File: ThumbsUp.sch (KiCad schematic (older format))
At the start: 138 parts, among them J1 Conn_01x04_Male, J10 Raiser_Male, J11 Raiser_Female, J12 Raiser_Male, J13 Raiser_Female, J14 Raiser_Male, J15 Raiser_Female, J16 Raiser_Male, J17 Raiser_Female, J18 Raiser_Male, J19 52559-1233, J2 Conn_01x04_Male, J20 Conn_01x04_Female, J21 Conn_01x04_Female, J22 Conn_01x04_Female, J23 Conn_01x04_Female, J24 Conn_01x04_Male, J25 Conn_01x04_Male, J26 Conn_01x04_Male, J27 Conn_01x04_Male, J28 Conn_01x04_Female, J29 Conn_01x04_Female, J3 Conn_01x04_Female, J30 Conn_01x04_Female, J31 Conn_01x04_Female, J4 Conn_01x04_Male, J5 Conn_01x04_Female, J6 Conn_01x04_Male, J7 Conn_01x04_Male, J8 Conn_01x04_Male, J9 Raiser_Female, SW1 SW_Push, U1 ATmega32U4-AU, Y1 16MHz

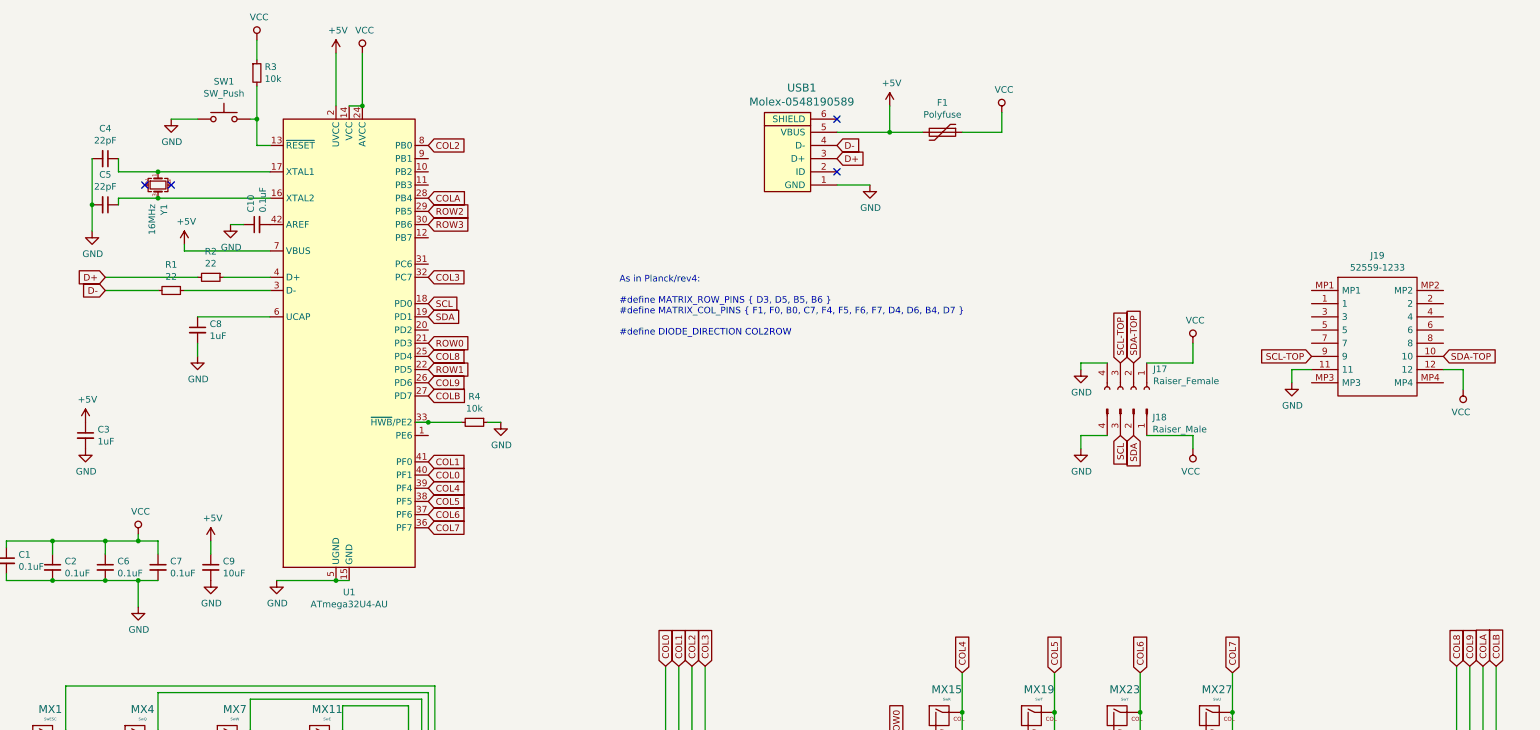
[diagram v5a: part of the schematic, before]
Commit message: Moved the tracks from under MCU
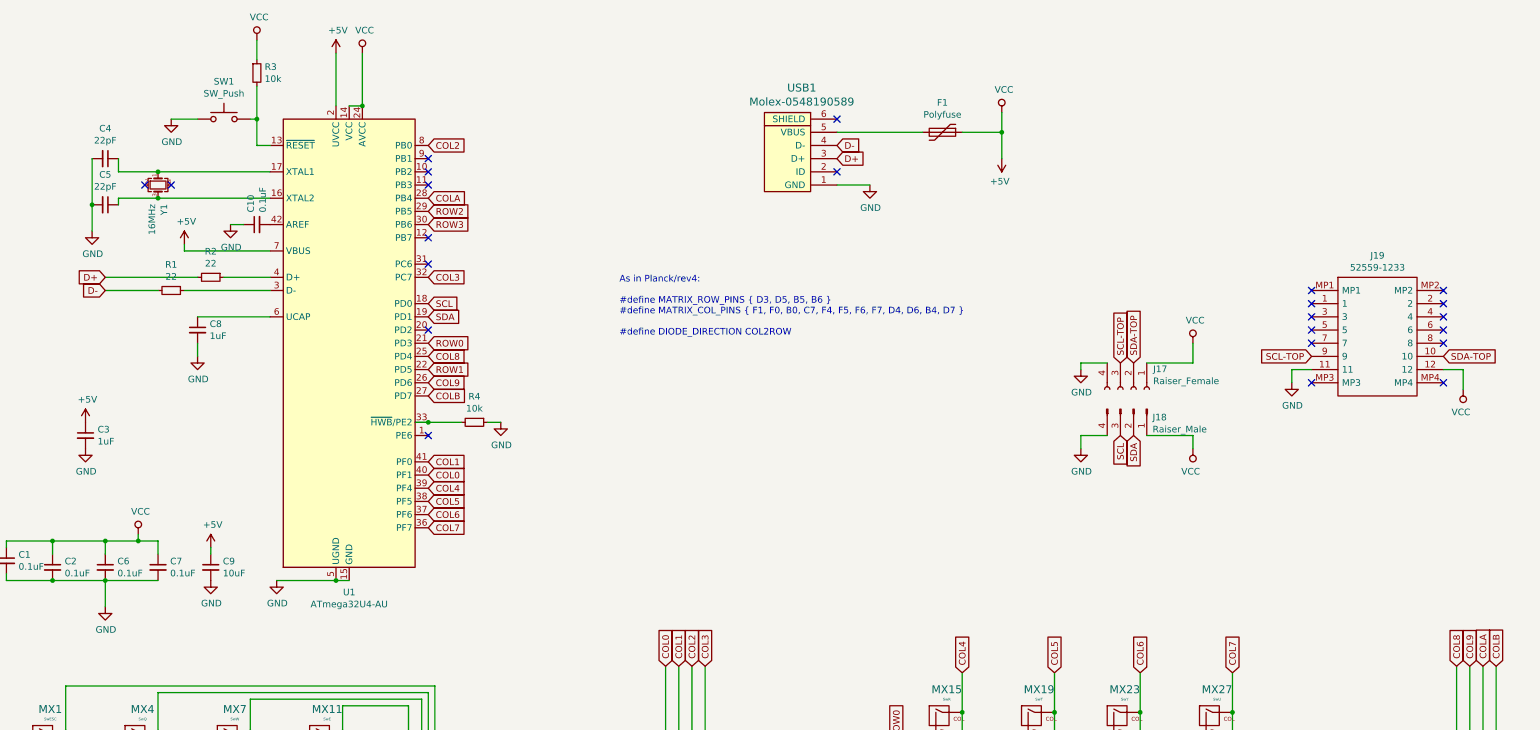
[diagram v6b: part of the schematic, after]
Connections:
- net VCC is gone; now on net +5V: C1.1, C2.1, C6.1, C7.1, F1.1, J17.1 (Pin_1), J18.1 (Pin_1), J19.12, R3.1, U1.14 (VCC), U1.24 (AVCC), U1.34 (VCC), U1.44 (AVCC)
- net +5V: no longer F1.2, USB1.5 (VBUS)
- new net: F1.2, USB1.5 (VBUS)
- no-connect marks 36 -> 55
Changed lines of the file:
@@
-	1    0    0    -1
-$EndComp
-$Comp
-L power:GND #PWR05
-U 1 1 616BEA7C
-P 2000 5750
-F 0 "#PWR05" H 2000 5500 50  0001 C CNN
-F 1 "GND" H 2005 5577 50  0000 C CNN
-F 2 "" H 2000 5750 50  0001 C CNN
-F 3 "" H 2000 5750 50  0001 C CNN
-	1    2000 5750
 	1    0    0    -1
 $EndComp
@@
 Connection ~ 2000 5250
 Wire Wire Line
-	2550 5250 2550 5350
-Wire Wire Line
-	2150 5550 2000 5550
-Wire Wire Line
-	2000 5550 2000 5750
-Wire Wire Line
-	2000 5550 1750 5550
-Connection ~ 2000 5550
+	2550 5300 2550 5350
 Wire Wire Line
 	1750 5550 1350 5550
@@
 $EndComp
 Wire Wire Line
-	7300 2150 7700 2150
-Wire Wire Line
-	7700 1950 7700 2150
-Connection ~ 7700 2150
-Wire Wire Line
-	7700 2150 7950 2150
+	8550 2350 8550 2150
 Wire Wire Line
 	8550 2000 8550 2150
@@
 	1    0    0    -1
 $EndComp
-Wire Wire Line
-	7300 2550 7550 2550
 Text GLabel 7300 2250 2    50   Input ~ 0
 D-
 Text GLabel 7300 2350 2    50   Input ~ 0
 D+
-Wire Wire Line
-	3700 1950 3600 1950
 Text GLabel 4200 3750 2    50   Input ~ 0
 ROW0
@@
 L power:+5V #PWR018
 U 1 1 61D515F6
-P 7700 1950
-F 0 "#PWR018" H 7700 1800 50  0001 C CNN
-F 1 "+5V" H 7715 2123 50  0000 C CNN
-F 2 "" H 7700 1950 50  0001 C CNN
-F 3 "" H 7700 1950 50  0001 C CNN
-	1    7700 1950
-	1    0    0    -1
+P 8550 2350
+F 0 "#PWR018" H 8550 2200 50  0001 C CNN
+F 1 "+5V" H 8565 2523 50  0000 C CNN
+F 2 "" H 8550 2350 50  0001 C CNN
+F 3 "" H 8550 2350 50  0001 C CNN
+	1    8550 2350
+	-1   0    0    1
 $EndComp
 $Comp
@@
 	1    0    0    -1
 $EndComp
-Wire Wire Line
-	3700 1550 3700 1950
 $Comp
 L power:VCC #PWR015
@@
 	1    0    0    -1
 $EndComp
-Wire Wire Line
-	3500 1550 3500 1950
 $Comp
 L power:VCC #PWR012
@@
 $EndComp
 Wire Wire Line
-	2350 3050 2350 3000
-Wire Wire Line
 	2350 3050 3000 3050
 $Comp
@@
 	1    0    0    -1
 $EndComp
-Wire Wire Line
-	2800 2850 2700 2850
 $Comp
 L power:GND #PWR016
@@
 L power:+5V #PWR09
 U 1 1 61E33E14
-P 2550 5250
-F 0 "#PWR09" H 2550 5100 50  0001 C CNN
-F 1 "+5V" H 2565 5423 50  0000 C CNN
-F 2 "" H 2550 5250 50  0001 C CNN
-F 3 "" H 2550 5250 50  0001 C CNN
-	1    2550 5250
+P 2550 5300
+F 0 "#PWR09" H 2550 5150 50  0001 C CNN
+F 1 "+5V" H 2565 5473 50  0000 C CNN
+F 2 "" H 2550 5300 50  0001 C CNN
+F 3 "" H 2550 5300 50  0001 C CNN
+	1    2550 5300
 	1    0    0    -1
 $EndComp
@@
 Connection ~ 4200 4350
 Wire Wire Line
-	3050 5550 3500 5550
-Wire Wire Line
-	3500 5550 3600 5550
-Connection ~ 3500 5550
-Connection ~ 3700 1950
-Wire Wire Line
 	4650 4350 4750 4350
 Wire Wire Line
@@
 	9650 4450 10000 4450
 Wire Wire Line
-	10000 4450 10000 4550
-Wire Wire Line
 	9350 3900 9150 3900
 Wire Wire Line
@@
 Wire Wire Line
 	9350 4450 9150 4450
-Wire Wire Line
-	9150 4450 9150 4550
 $Comp
 L Connector:Conn_01x04_Male J7
@@
 Wire Wire Line
 	10300 6550 10300 7350
+Wire Wire Line
+	7300 2150 7950 2150
+Connection ~ 8550 2150
+NoConn ~ 4200 2350
+NoConn ~ 4200 2450
+NoConn ~ 4200 2550
+NoConn ~ 4200 2950
+NoConn ~ 4200 3150
+NoConn ~ 4200 3650
+NoConn ~ 4200 4450
+NoConn ~ 11900 3350
+NoConn ~ 11900 3450
+NoConn ~ 11900 3550
+NoConn ~ 11900 3650
+NoConn ~ 11900 3750
+NoConn ~ 11900 4050
+NoConn ~ 10900 3350
+NoConn ~ 10900 3450
+NoConn ~ 10900 3550
+NoConn ~ 10900 3650
+NoConn ~ 10900 3750
+NoConn ~ 10900 4050
+Wire Wire Line
+	3050 5550 3500 5550
+Connection ~ 3500 5550
+Wire Wire Line
+	3500 5550 3600 5550
+Wire Wire Line
+	3700 1550 3700 1950
+Wire Wire Line
+	3700 1950 3600 1950
+Connection ~ 3700 1950
+Wire Wire Line
+	1750 5550 2150 5550
+$Comp
+L power:GND #PWR05
+U 1 1 616BEA7C
+P 1750 5750
+F 0 "#PWR05" H 1750 5500 50  0001 C CNN
+F 1 "GND" H 1755 5577 50  0000 C CNN
+F 2 "" H 1750 5750 50  0001 C CNN
+F 3 "" H 1750 5750 50  0001 C CNN
+	1    1750 5750
+	1    0    0    -1
+$EndComp
+Wire Wire Line
+	1750 5750 1750 5550
+Wire Wire Line
+	7300 2550 7550 2550
+Wire Wire Line
+	10000 4450 10000 4550
+Wire Wire Line
+	9150 4450 9150 4550
+Wire Wire Line
+	3500 1550 3500 1950
+Wire Wire Line
+	2350 3050 2350 3000
+Wire Wire Line
+	2700 2850 2800 2850
 $EndSCHEMATC

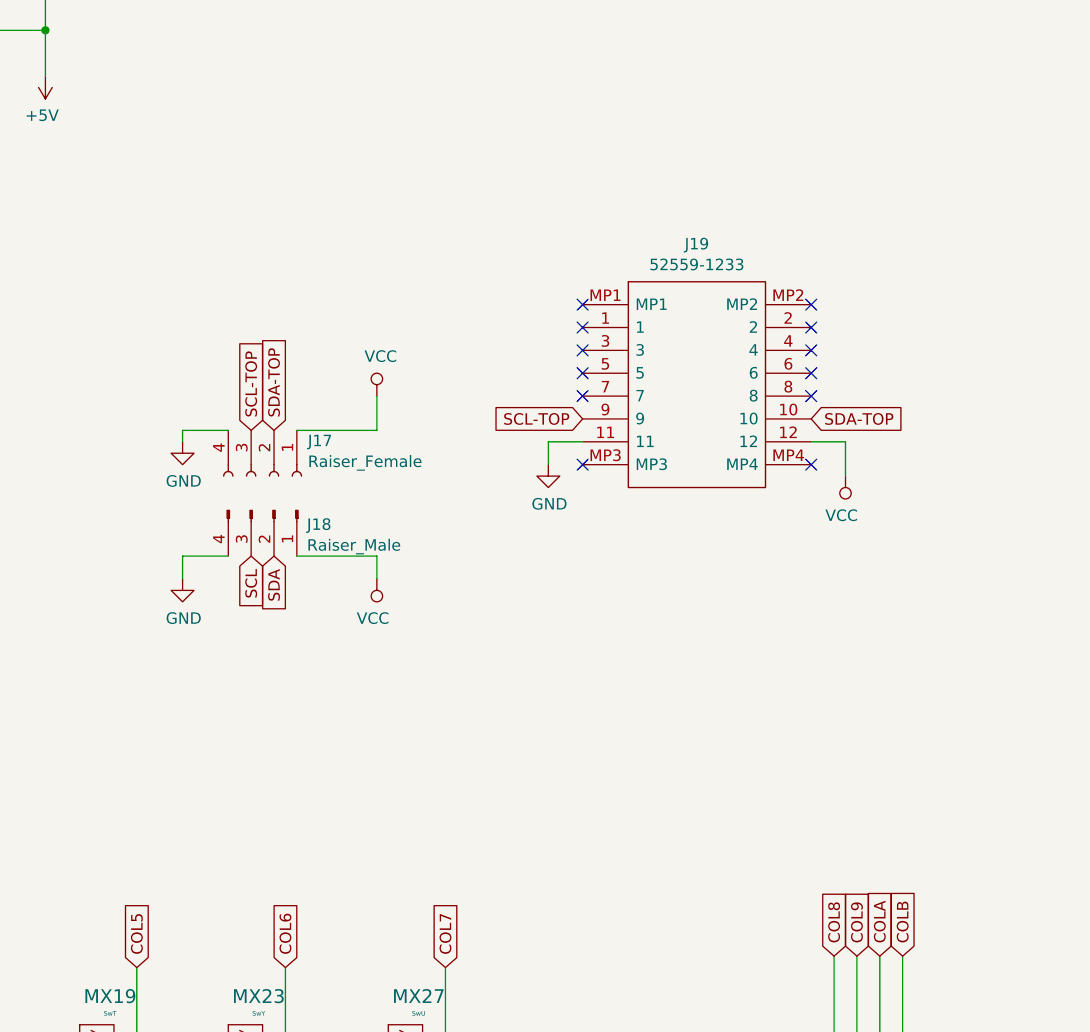
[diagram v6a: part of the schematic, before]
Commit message: Moved the tracks from under MCU
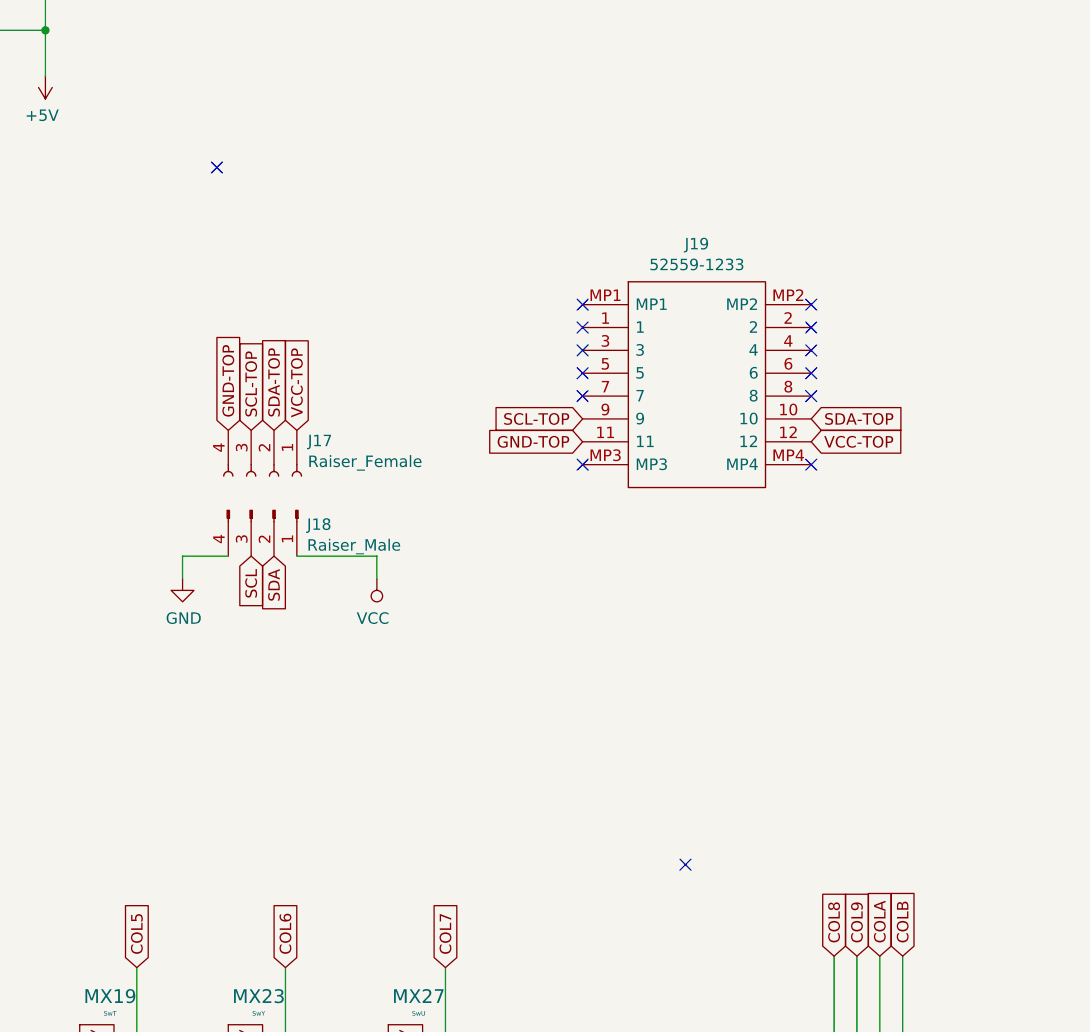
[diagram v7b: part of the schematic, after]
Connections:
- net +5V: no longer J17.1 (Pin_1), J19.12
- net GND: no longer J17.4 (Pin_4), J19.11
- new net GND-TOP: J17.4 (Pin_4), J19.11
- new net VCC-TOP: J17.1 (Pin_1), J19.12
- no-connect marks 55 -> 57
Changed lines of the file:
@@
 Text GLabel 11900 3850 2    50   Input ~ 0
 SDA-TOP
-$Comp
-L power:VCC #PWR0101
-U 1 1 634EB4E1
-P 12050 4100
-F 0 "#PWR0101" H 12050 3950 50  0001 C CNN
-F 1 "VCC" H 12067 4273 50  0000 C CNN
-F 2 "" H 12050 4100 50  0001 C CNN
-F 3 "" H 12050 4100 50  0001 C CNN
-	1    12050 4100
-	-1   0    0    1
-$EndComp
-Wire Wire Line
-	11900 3950 12050 3950
-Wire Wire Line
-	12050 3950 12050 4100
-$Comp
-L power:GND #PWR0102
-U 1 1 6355E41C
-P 10750 4050
-F 0 "#PWR0102" H 10750 3800 50  0001 C CNN
-F 1 "GND" H 10755 3877 50  0000 C CNN
-F 2 "" H 10750 4050 50  0001 C CNN
-F 3 "" H 10750 4050 50  0001 C CNN
-	1    10750 4050
-	1    0    0    -1
-$EndComp
-Wire Wire Line
-	10750 4050 10750 3950
-Wire Wire Line
-	10750 3950 10900 3950
 Text GLabel 4200 3450 2    50   Input ~ 0
 SCL
@@
 $EndComp
 $Comp
-L power:GND #PWR0104
-U 1 1 6362B3DF
-P 9150 3950
-F 0 "#PWR0104" H 9150 3700 50  0001 C CNN
-F 1 "GND" H 9155 3777 50  0000 C CNN
-F 2 "" H 9150 3950 50  0001 C CNN
-F 3 "" H 9150 3950 50  0001 C CNN
-	1    9150 3950
-	1    0    0    -1
-$EndComp
-$Comp
 L power:VCC #PWR0105
 U 1 1 6362B8F1
@@
 	-1   0    0    1
 $EndComp
-$Comp
-L power:VCC #PWR0106
-U 1 1 6362C88F
-P 10000 3750
-F 0 "#PWR0106" H 10000 3600 50  0001 C CNN
-F 1 "VCC" H 10017 3923 50  0000 C CNN
-F 2 "" H 10000 3750 50  0001 C CNN
-F 3 "" H 10000 3750 50  0001 C CNN
-	1    10000 3750
-	1    0    0    -1
-$EndComp
-Wire Wire Line
-	9650 3900 10000 3900
-Wire Wire Line
-	10000 3900 10000 3750
 Wire Wire Line
 	9650 4450 10000 4450
-Wire Wire Line
-	9350 3900 9150 3900
-Wire Wire Line
-	9150 3900 9150 3950
 Wire Wire Line
 	9350 4450 9150 4450
@@
 Wire Wire Line
 	2700 2850 2800 2850
+Text GLabel 11900 3950 2    50   Input ~ 0
+VCC-TOP
+Text GLabel 9650 3900 1    50   Input ~ 0
+VCC-TOP
+NoConn ~ 11350 5800
+Text GLabel 10900 3950 0    50   Input ~ 0
+GND-TOP
+Text GLabel 9350 3900 1    50   Input ~ 0
+GND-TOP
+NoConn ~ 9300 2750
 $EndSCHEMATC

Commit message: Redrew the middle board
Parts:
- J19: symbol 52559-1233:52559-1233 -> ThumbsUp-rescue:52559-1233-52559-1233
- MX1, MX10, MX11, MX12, MX13, MX14, MX15, MX16, MX17, MX18, MX19, MX2, MX20, MX21, MX22, MX23, MX24, MX25, MX26, MX27, MX28, MX29, MX3, MX30, MX31, MX32, MX33, MX34, MX35, MX36, MX37, MX38, MX39, MX4, MX40, MX41, MX42, MX43, MX44, MX5, MX6, MX7, MX8, MX9: symbol MX_Alps_Hybrid:MX-NoLED -> ThumbsUp-rescue:MX-NoLED-MX_Alps_Hybrid
- USB1: symbol random-keyboard-parts:Molex-0548190589 -> ThumbsUp-rescue:Molex-0548190589-random-keyboard-parts
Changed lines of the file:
@@
 D-
 $Comp
-L random-keyboard-parts:Molex-0548190589 USB1
+L ThumbsUp-rescue:Molex-0548190589-random-keyboard-parts USB1
 U 1 1 616D7FEE
 P 7000 2350
@@
 $EndComp
 $Comp
-L MX_Alps_Hybrid:MX-NoLED MX1
+L ThumbsUp-rescue:MX-NoLED-MX_Alps_Hybrid MX1
 U 1 1 61FB95FB
 P 1300 6750
@@
 $EndComp
 $Comp
-L MX_Alps_Hybrid:MX-NoLED MX4
+L ThumbsUp-rescue:MX-NoLED-MX_Alps_Hybrid MX4
 U 1 1 61FB9608
 P 2000 6750
@@
 $EndComp
 $Comp
-L MX_Alps_Hybrid:MX-NoLED MX2
+L ThumbsUp-rescue:MX-NoLED-MX_Alps_Hybrid MX2
 U 1 1 61FB9615
 P 1300 7550
@@
 $EndComp
 $Comp
-L MX_Alps_Hybrid:MX-NoLED MX7
+L ThumbsUp-rescue:MX-NoLED-MX_Alps_Hybrid MX7
 U 1 1 61FB962F
 P 2700 6750
@@
 $EndComp
 $Comp
-L MX_Alps_Hybrid:MX-NoLED MX11
+L ThumbsUp-rescue:MX-NoLED-MX_Alps_Hybrid MX11
 U 1 1 61FB963C
 P 3400 6750
@@
 $EndComp
 $Comp
-L MX_Alps_Hybrid:MX-NoLED MX8
+L ThumbsUp-rescue:MX-NoLED-MX_Alps_Hybrid MX8
 U 1 1 61FB9649
 P 2700 7550
@@
 $EndComp
 $Comp
-L MX_Alps_Hybrid:MX-NoLED MX12
+L ThumbsUp-rescue:MX-NoLED-MX_Alps_Hybrid MX12
 U 1 1 61FB9656
 P 3400 7550
@@
 $EndComp
 $Comp
-L MX_Alps_Hybrid:MX-NoLED MX3
+L ThumbsUp-rescue:MX-NoLED-MX_Alps_Hybrid MX3
 U 1 1 61FB9663
 P 1300 8350
@@
 $EndComp
 $Comp
-L MX_Alps_Hybrid:MX-NoLED MX6
+L ThumbsUp-rescue:MX-NoLED-MX_Alps_Hybrid MX6
 U 1 1 61FB9670
 P 2000 8350
@@
 $EndComp
 $Comp
-L MX_Alps_Hybrid:MX-NoLED MX9
+L ThumbsUp-rescue:MX-NoLED-MX_Alps_Hybrid MX9
 U 1 1 61FB9696
 P 2700 8350
@@
 $EndComp
 $Comp
-L MX_Alps_Hybrid:MX-NoLED MX13
+L ThumbsUp-rescue:MX-NoLED-MX_Alps_Hybrid MX13
 U 1 1 61FB96A3
 P 3400 8350
@@
 $EndComp
 $Comp
-L MX_Alps_Hybrid:MX-NoLED MX10
+L ThumbsUp-rescue:MX-NoLED-MX_Alps_Hybrid MX10
 U 1 1 61FB96B0
 P 2700 9150
@@
 $EndComp
 $Comp
-L MX_Alps_Hybrid:MX-NoLED MX21
+L ThumbsUp-rescue:MX-NoLED-MX_Alps_Hybrid MX21
 U 1 1 62015099
 P 8800 8200
@@
 $EndComp
 $Comp
-L MX_Alps_Hybrid:MX-NoLED MX17
+L ThumbsUp-rescue:MX-NoLED-MX_Alps_Hybrid MX17
 U 1 1 6201508C
 P 8100 8200
@@
 $EndComp
 $Comp
-L MX_Alps_Hybrid:MX-NoLED MX20
+L ThumbsUp-rescue:MX-NoLED-MX_Alps_Hybrid MX20
 U 1 1 6201507F
 P 8800 7400
@@
 $EndComp
 $Comp
-L MX_Alps_Hybrid:MX-NoLED MX16
+L ThumbsUp-rescue:MX-NoLED-MX_Alps_Hybrid MX16
 U 1 1 62015072
 P 8100 7400
@@
 $EndComp
 $Comp
-L MX_Alps_Hybrid:MX-NoLED MX19
+L ThumbsUp-rescue:MX-NoLED-MX_Alps_Hybrid MX19
 U 1 1 62015065
 P 8800 6600
@@
 $EndComp
 $Comp
-L MX_Alps_Hybrid:MX-NoLED MX15
+L ThumbsUp-rescue:MX-NoLED-MX_Alps_Hybrid MX15
 U 1 1 62015058
 P 8100 6600
@@
 $EndComp
 $Comp
-L MX_Alps_Hybrid:MX-NoLED MX29
+L ThumbsUp-rescue:MX-NoLED-MX_Alps_Hybrid MX29
 U 1 1 61713053
 P 10150 8200
@@
 $EndComp
 $Comp
-L MX_Alps_Hybrid:MX-NoLED MX25
+L ThumbsUp-rescue:MX-NoLED-MX_Alps_Hybrid MX25
 U 1 1 61713046
 P 9450 8200
@@
 $EndComp
 $Comp
-L MX_Alps_Hybrid:MX-NoLED MX28
+L ThumbsUp-rescue:MX-NoLED-MX_Alps_Hybrid MX28
 U 1 1 616E98B3
 P 10150 7400
@@
 $EndComp
 $Comp
-L MX_Alps_Hybrid:MX-NoLED MX24
+L ThumbsUp-rescue:MX-NoLED-MX_Alps_Hybrid MX24
 U 1 1 616E989E
 P 9450 7400
@@
 $EndComp
 $Comp
-L MX_Alps_Hybrid:MX-NoLED MX27
+L ThumbsUp-rescue:MX-NoLED-MX_Alps_Hybrid MX27
 U 1 1 616E6A1E
 P 10150 6600
@@
 $EndComp
 $Comp
-L MX_Alps_Hybrid:MX-NoLED MX23
+L ThumbsUp-rescue:MX-NoLED-MX_Alps_Hybrid MX23
 U 1 1 616E00A7
 P 9450 6600
@@
 	4050 6500 4050 7100
 $Comp
-L MX_Alps_Hybrid:MX-NoLED MX5
+L ThumbsUp-rescue:MX-NoLED-MX_Alps_Hybrid MX5
 U 1 1 61FB9622
 P 2000 7550
@@
 	7600 9200 7750 9200
 $Comp
-L MX_Alps_Hybrid:MX-NoLED MX42
+L ThumbsUp-rescue:MX-NoLED-MX_Alps_Hybrid MX42
 U 1 1 6261980F
 P 17000 6750
@@
 $EndComp
 $Comp
-L MX_Alps_Hybrid:MX-NoLED MX39
+L ThumbsUp-rescue:MX-NoLED-MX_Alps_Hybrid MX39
 U 1 1 62619815
 P 16300 6750
@@
 $EndComp
 $Comp
-L MX_Alps_Hybrid:MX-NoLED MX43
+L ThumbsUp-rescue:MX-NoLED-MX_Alps_Hybrid MX43
 U 1 1 6261981B
 P 17000 7550
@@
 $EndComp
 $Comp
-L MX_Alps_Hybrid:MX-NoLED MX35
+L ThumbsUp-rescue:MX-NoLED-MX_Alps_Hybrid MX35
 U 1 1 62619821
 P 15600 6750
@@
 $EndComp
 $Comp
-L MX_Alps_Hybrid:MX-NoLED MX31
+L ThumbsUp-rescue:MX-NoLED-MX_Alps_Hybrid MX31
 U 1 1 62619827
 P 14900 6750
@@
 $EndComp
 $Comp
-L MX_Alps_Hybrid:MX-NoLED MX36
+L ThumbsUp-rescue:MX-NoLED-MX_Alps_Hybrid MX36
 U 1 1 6261982D
 P 15600 7550
@@
 $EndComp
 $Comp
-L MX_Alps_Hybrid:MX-NoLED MX32
+L ThumbsUp-rescue:MX-NoLED-MX_Alps_Hybrid MX32
 U 1 1 62619833
 P 14900 7550
@@
 $EndComp
 $Comp
-L MX_Alps_Hybrid:MX-NoLED MX44
+L ThumbsUp-rescue:MX-NoLED-MX_Alps_Hybrid MX44
 U 1 1 62619839
 P 17000 8350
@@
 $EndComp
 $Comp
-L MX_Alps_Hybrid:MX-NoLED MX41
+L ThumbsUp-rescue:MX-NoLED-MX_Alps_Hybrid MX41
 U 1 1 6261983F
 P 16300 8350
@@
 $EndComp
 $Comp
-L MX_Alps_Hybrid:MX-NoLED MX37
+L ThumbsUp-rescue:MX-NoLED-MX_Alps_Hybrid MX37
 U 1 1 62619845
 P 15600 8350
@@
 $EndComp
 $Comp
-L MX_Alps_Hybrid:MX-NoLED MX33
+L ThumbsUp-rescue:MX-NoLED-MX_Alps_Hybrid MX33
 U 1 1 6261984B
 P 14900 8350
@@
 $EndComp
 $Comp
-L MX_Alps_Hybrid:MX-NoLED MX34
+L ThumbsUp-rescue:MX-NoLED-MX_Alps_Hybrid MX34
 U 1 1 6261985D
 P 14900 9150
@@
 $EndComp
 $Comp
-L MX_Alps_Hybrid:MX-NoLED MX38
+L ThumbsUp-rescue:MX-NoLED-MX_Alps_Hybrid MX38
 U 1 1 62619863
 P 15600 9150
@@
 	14250 6500 14250 7100
 $Comp
-L MX_Alps_Hybrid:MX-NoLED MX40
+L ThumbsUp-rescue:MX-NoLED-MX_Alps_Hybrid MX40
 U 1 1 6261988C
 P 16300 7550
@@
 Connection ~ 7750 9200
 $Comp
-L MX_Alps_Hybrid:MX-NoLED MX22
+L ThumbsUp-rescue:MX-NoLED-MX_Alps_Hybrid MX22
 U 1 1 62882FE4
 P 8850 11000
@@
 $EndComp
 $Comp
-L MX_Alps_Hybrid:MX-NoLED MX18
+L ThumbsUp-rescue:MX-NoLED-MX_Alps_Hybrid MX18
 U 1 1 62882FEA
 P 8150 11000
@@
 	8550 10950 8700 10950
 $Comp
-L MX_Alps_Hybrid:MX-NoLED MX30
+L ThumbsUp-rescue:MX-NoLED-MX_Alps_Hybrid MX30
 U 1 1 62A1D5C7
 P 10600 11050
@@
 $EndComp
 $Comp
-L MX_Alps_Hybrid:MX-NoLED MX26
+L ThumbsUp-rescue:MX-NoLED-MX_Alps_Hybrid MX26
 U 1 1 62A1D5CD
 P 9900 11050
@@
 Connection ~ 6200 7000
 $Comp
-L MX_Alps_Hybrid:MX-NoLED MX14
+L ThumbsUp-rescue:MX-NoLED-MX_Alps_Hybrid MX14
 U 1 1 61FB96BD
 P 3400 9150
@@
 	14750 7500 14750 8300
 $Comp
-L 52559-1233:52559-1233 J19
+L ThumbsUp-rescue:52559-1233-52559-1233 J19
 U 1 1 634DD7F1
 P 10900 3350
